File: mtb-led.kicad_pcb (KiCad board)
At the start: 2 copper layers, 120 x 50 mm, 57 parts, among them J7 AVR-ISP-6, J9 DEBUG, SW1 SW_Push, U1 ATmega328PB-A, U2 78M05, U3 TLC5940PWP, U4 TLC5940PWP, U5 MAX487E, Y1 14.7456 MHz

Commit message: Rename outputs according to PCB design.
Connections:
- J3 pad 2: /OUT15 -> /OUT23
- J3 pad 3: /OUT14 -> /OUT22
- J3 pad 4: /OUT13 -> /OUT21
- J3 pad 5: /OUT12 -> /OUT20
- J3 pad 6: /OUT11 -> /OUT19
- J3 pad 7: /OUT10 -> /OUT18
- J3 pad 8: /OUT9 -> /OUT17
- J3 pad 9: /OUT8 -> /OUT16
- J4 pad 2: /OUT7 -> /OUT15
- J4 pad 3: /OUT6 -> /OUT14
- J4 pad 4: /OUT5 -> /OUT13
- J4 pad 5: /OUT4 -> /OUT12
- J4 pad 6: /OUT3 -> /OUT11
- J4 pad 7: /OUT2 -> /OUT10
- J4 pad 8: /OUT1 -> /OUT9
- J4 pad 9: /OUT0 -> /OUT8
- J5 pad 2: /OUT31 -> /OUT7
- J5 pad 3: /OUT30 -> /OUT6
- J5 pad 4: /OUT29 -> /OUT5
- J5 pad 5: /OUT28 -> /OUT4
- J5 pad 6: /OUT27 -> /OUT3
- J5 pad 7: /OUT26 -> /OUT2
- J5 pad 8: /OUT25 -> /OUT1
- J5 pad 9: /OUT24 -> /OUT0
- J6 pad 2: /OUT23 -> /OUT31
- J6 pad 3: /OUT22 -> /OUT30
- J6 pad 4: /OUT21 -> /OUT29
- J6 pad 5: /OUT20 -> /OUT28
- J6 pad 6: /OUT19 -> /OUT27
- J6 pad 7: /OUT18 -> /OUT26
- J6 pad 8: /OUT17 -> /OUT25
- J6 pad 9: /OUT16 -> /OUT24
- U3 pad 10: /OUT3 -> /OUT11
- U3 pad 11: /OUT4 -> /OUT12
- U3 pad 12: /OUT5 -> /OUT13
- U3 pad 13: /OUT6 -> /OUT14
- U3 pad 14: /OUT7 -> /OUT15
- U3 pad 15: /OUT8 -> /OUT16
- U3 pad 16: /OUT9 -> /OUT17
- U3 pad 17: /OUT10 -> /OUT18
- U3 pad 18: /OUT11 -> /OUT19
- U3 pad 19: /OUT12 -> /OUT20
- U3 pad 20: /OUT13 -> /OUT21
- U3 pad 21: /OUT14 -> /OUT22
- U3 pad 22: /OUT15 -> /OUT23
- U3 pad 7: /OUT0 -> /OUT8
- U3 pad 8: /OUT1 -> /OUT9
- U3 pad 9: /OUT2 -> /OUT10
- U4 pad 10: /OUT19 -> /OUT27
- U4 pad 11: /OUT20 -> /OUT28
- U4 pad 12: /OUT21 -> /OUT29
- U4 pad 13: /OUT22 -> /OUT30
- U4 pad 14: /OUT23 -> /OUT31
- U4 pad 15: /OUT24 -> /OUT0
- U4 pad 16: /OUT25 -> /OUT1
- U4 pad 17: /OUT26 -> /OUT2
- U4 pad 18: /OUT27 -> /OUT3
- U4 pad 19: /OUT28 -> /OUT4
- U4 pad 20: /OUT29 -> /OUT5
- U4 pad 21: /OUT30 -> /OUT6
- U4 pad 22: /OUT31 -> /OUT7
- U4 pad 7: /OUT16 -> /OUT24
- U4 pad 8: /OUT17 -> /OUT25
- U4 pad 9: /OUT18 -> /OUT26
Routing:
- net /OUT25: track 17.1 -> 22.9 mm
- net /OUT17: track 22.9 -> 17.6 mm
- net /OUT14: track 21.7 -> 16.5 mm
- net /OUT15: track 24.3 -> 19.2 mm
- net /OUT13: track 20.3 -> 15.3 mm
- net /OUT24: track 19.7 -> 24.5 mm
- net /OUT26: track 15.9 -> 20.2 mm
- net /OUT0: track 23.8 -> 19.7 mm
- net /OUT6: track 16.5 -> 20.4 mm
- net /OUT21: track 16.4 -> 20.3 mm
- net /OUT18: track 20.2 -> 16.4 mm
- net /OUT7: track 19.2 -> 22.8 mm
- net /OUT1: track 20.6 -> 17.1 mm
- net /OUT16: track 24.5 -> 21.0 mm
- net /OUT23: track 21.0 -> 24.3 mm
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
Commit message: Add OSHW logo & web page url.
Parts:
- added REF**: OSHW-Logo_7.5x8mm_SilkScreen, Symbol:OSHW-Logo_7.5x8mm_SilkScreen, F.Cu at (155.4, 88.1)
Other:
- board text added: "https://mtb.kmz-brno.cz/"

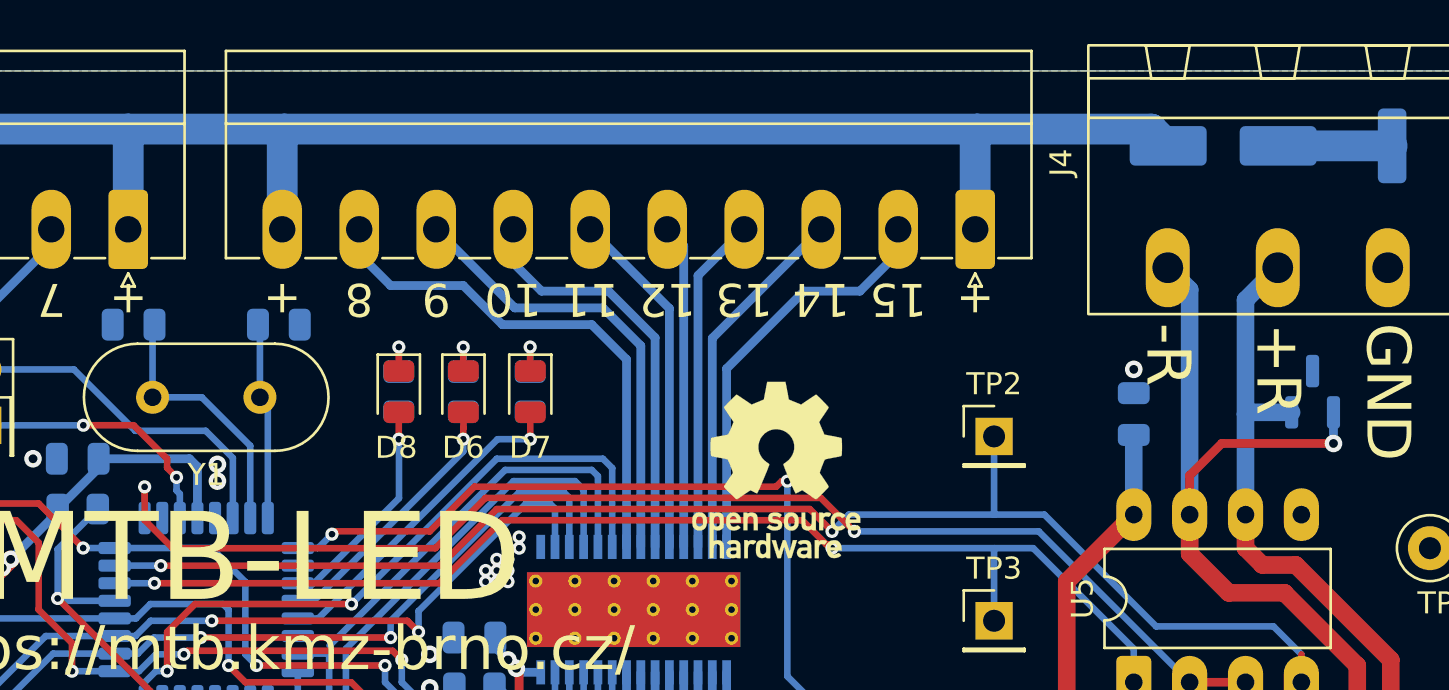
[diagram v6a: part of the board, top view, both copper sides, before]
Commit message: Add capacitor to +12V.
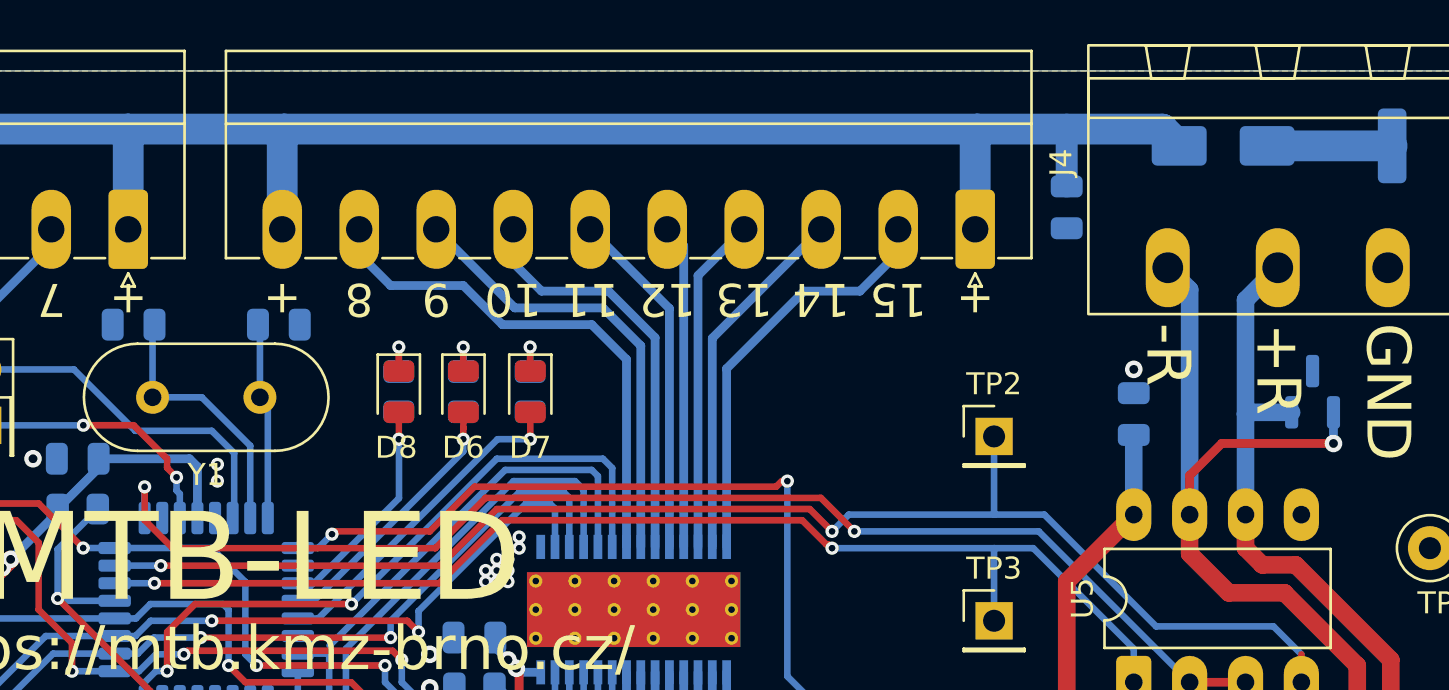
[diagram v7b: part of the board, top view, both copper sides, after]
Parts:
- removed REF**: OSHW-Logo_7.5x8mm_SilkScreen, Symbol:OSHW-Logo_7.5x8mm_SilkScreen
- added C12: 22u/25V, Capacitor_SMD:C_0805_2012Metric, B.Cu at (168.7, 76.2)
- D5: footprint Diode_SMD:D_SMA_Handsoldering -> Diode_SMD:D_SMA
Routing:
- net +12V: track 232.5 -> 235.6 mm
